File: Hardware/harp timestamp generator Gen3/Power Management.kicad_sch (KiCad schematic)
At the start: 36 parts, among them IC1 MCP73831, IC4 TPS2114, IC5 LP5951MFX-3.3/NOPB, Q1 RTU002P02T106, Q2 BC817-40W, Q3 SBC817, Q4 DMG1012UW, Q5 DMP2035U-7, X1 B2B-XH-A(LF)(SN)

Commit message: review após 1ª produção de placas teste
> harp timestamp generator Gen3
  . mudança da case de Q2
  . mudança de ligação em 'Button0'

> harp timestamp generator Gen3 front panel
  . acerto no recorte da ficha IDC e interruptor bateria
  . modificação de setup no logo 'harp'

> harp timestamp generator Gen3 rear panel
  . acerto no recorte de ficha USB
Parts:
- Q2: footprint Package_TO_SOT_SMD:SOT-23 -> Package_TO_SOT_SMD:SOT-323_SC-70
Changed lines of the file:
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@@
 			)
 		)
-		(property "Footprint" "Package_TO_SOT_SMD:SOT-23"
+		(property "Footprint" "Package_TO_SOT_SMD:SOT-323_SC-70"
 			(at 144.78 115.57 0)
 			(hide yes)

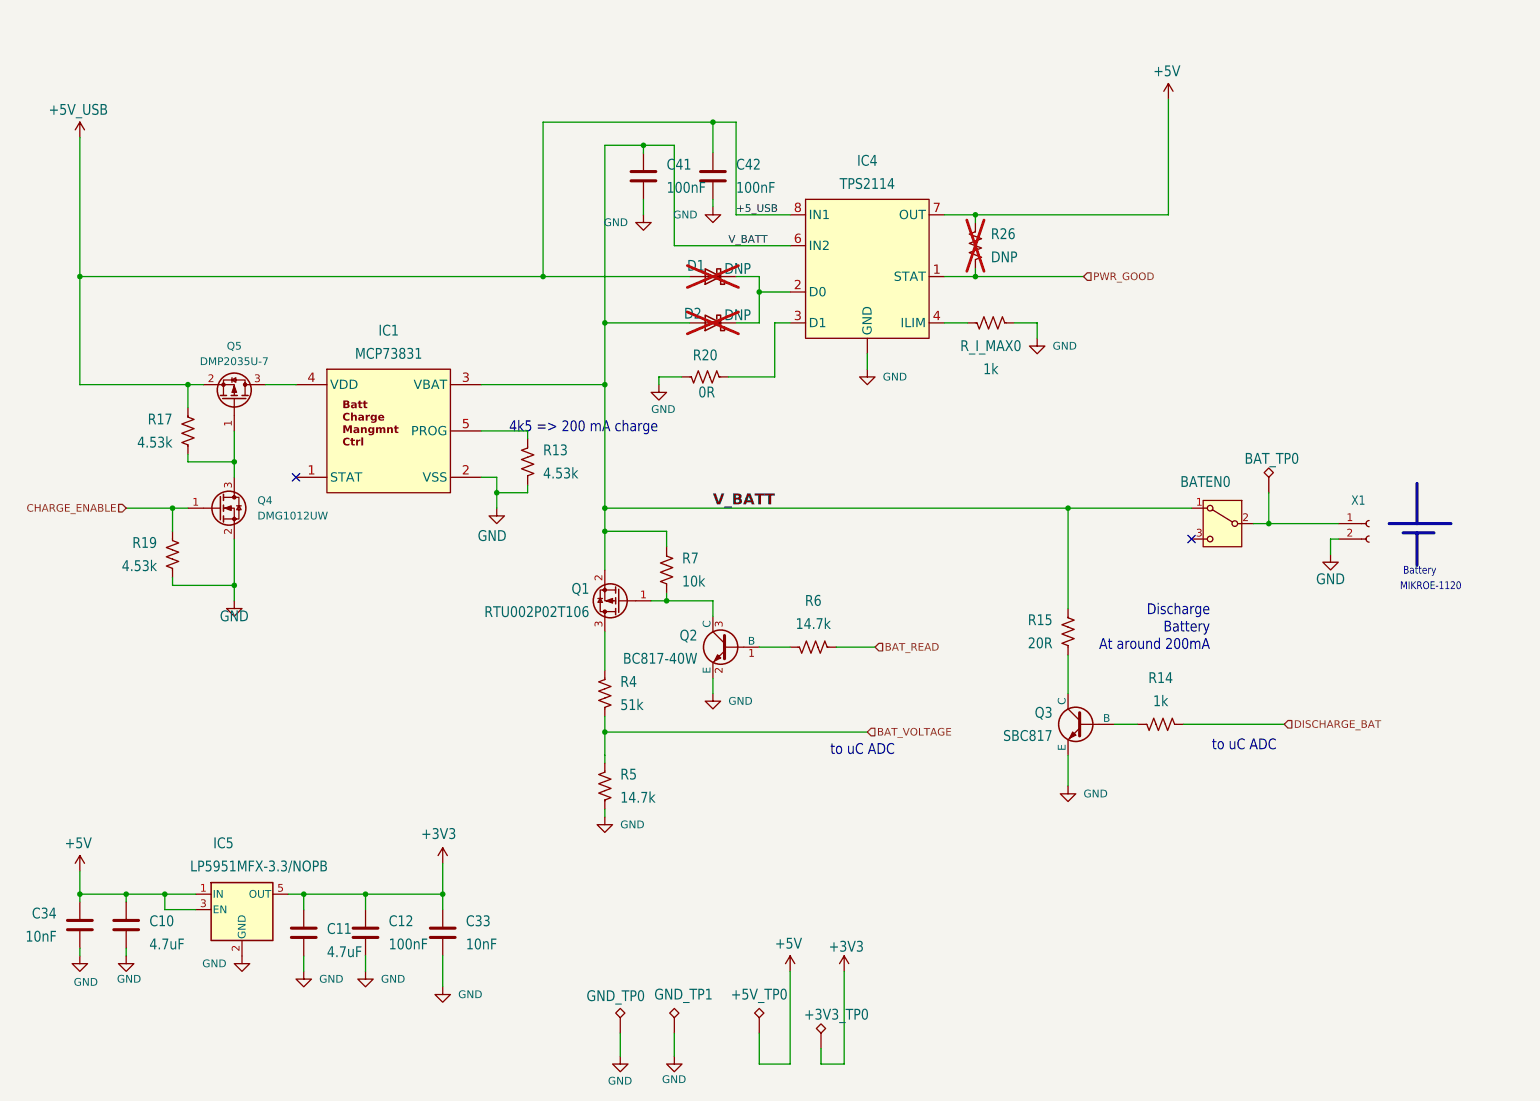
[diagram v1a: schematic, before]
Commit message: em passo de desenvolvimento Power-Select & Battery Protection
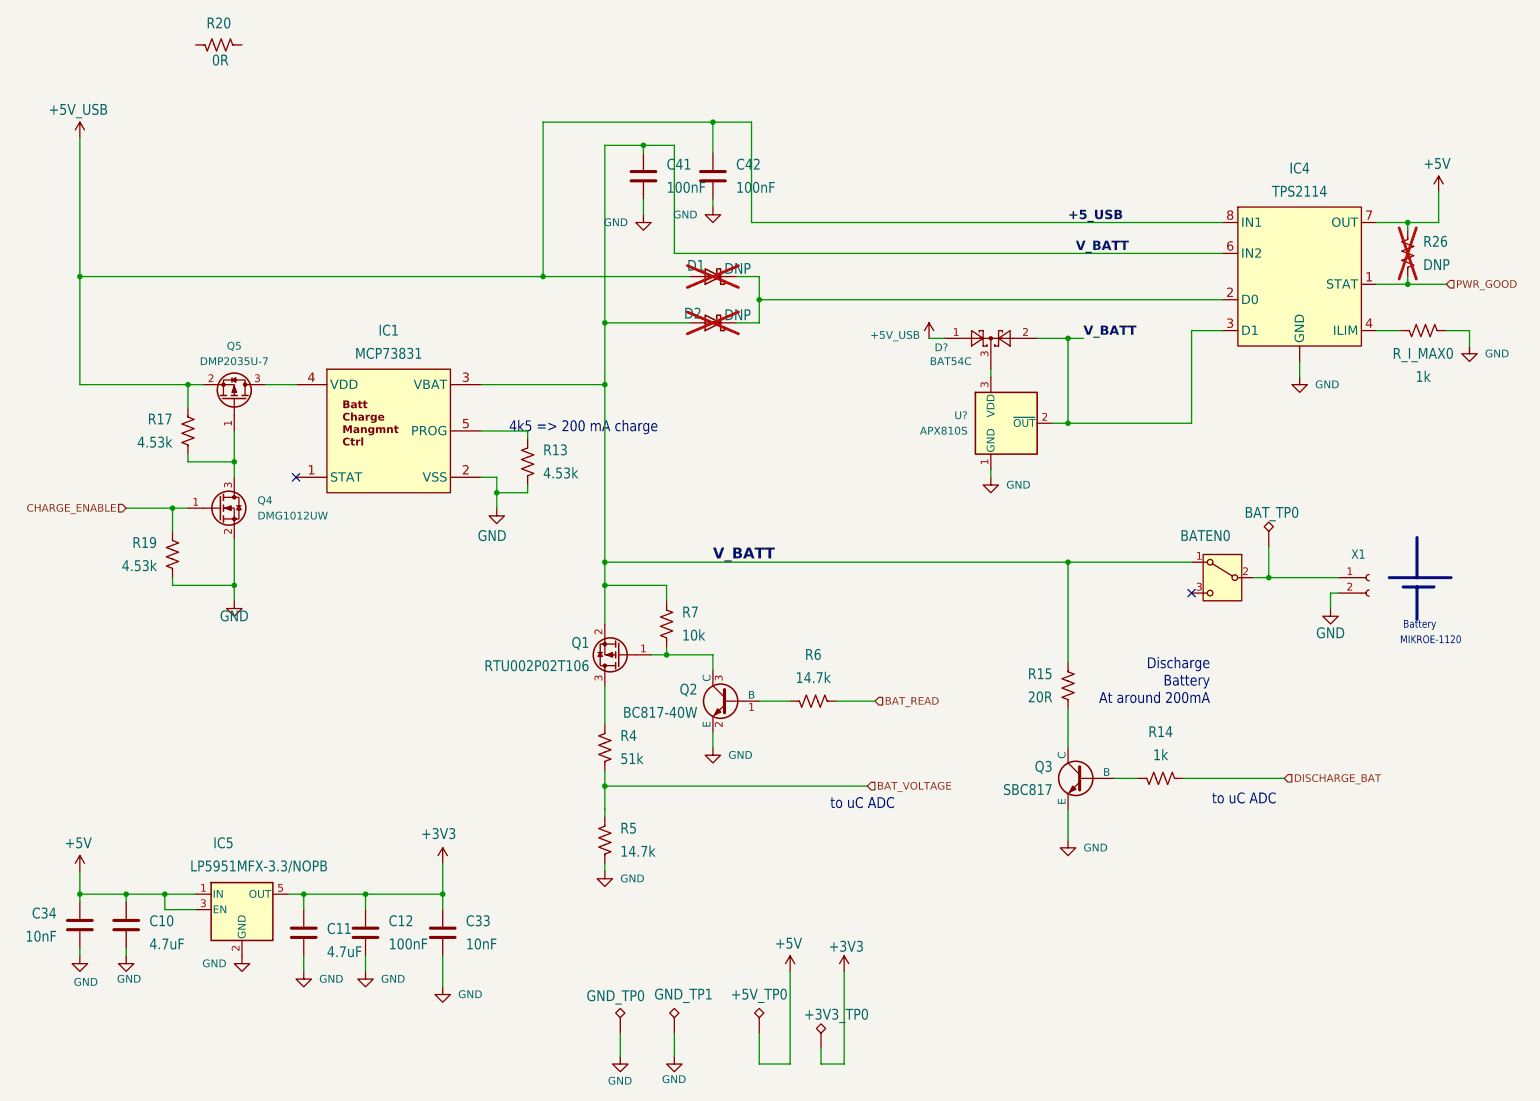
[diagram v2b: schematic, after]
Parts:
- added D?: BAT54C, Package_TO_SOT_SMD:SOT-23, symbol Diode:BAT54C
- added U?: APX810S, Package_TO_SOT_SMD:SOT-23, symbol harp_timestamp_generator_Gen3:APX810S
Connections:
- net +5V_USB: now also D?.1
- net GND: now also U?.1 (GND); no longer R20.1
- net V_BATT: now also IC4.3 (D1), D?.2, U?.2 (~{OUT})
- net at R20.2: no longer IC4.3 (D1)
- new net: D?.3, U?.3 (VDD)
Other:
- moved on the sheet: BATEN0, BAT_TP0, IC4, Q1, Q2, Q3, R14, R15, R20, R26, R4, R5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
